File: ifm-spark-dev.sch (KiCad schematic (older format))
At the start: 21 parts, among them J1 CONN_01X03_MALE, J2 CONN_01X06, J3 CONN_01X02, J4 CONN_01X07, J5 CONN_01X03_MALE, SW1 PTS525-SM15, U1 STM32F030x4, Y1 8MHz

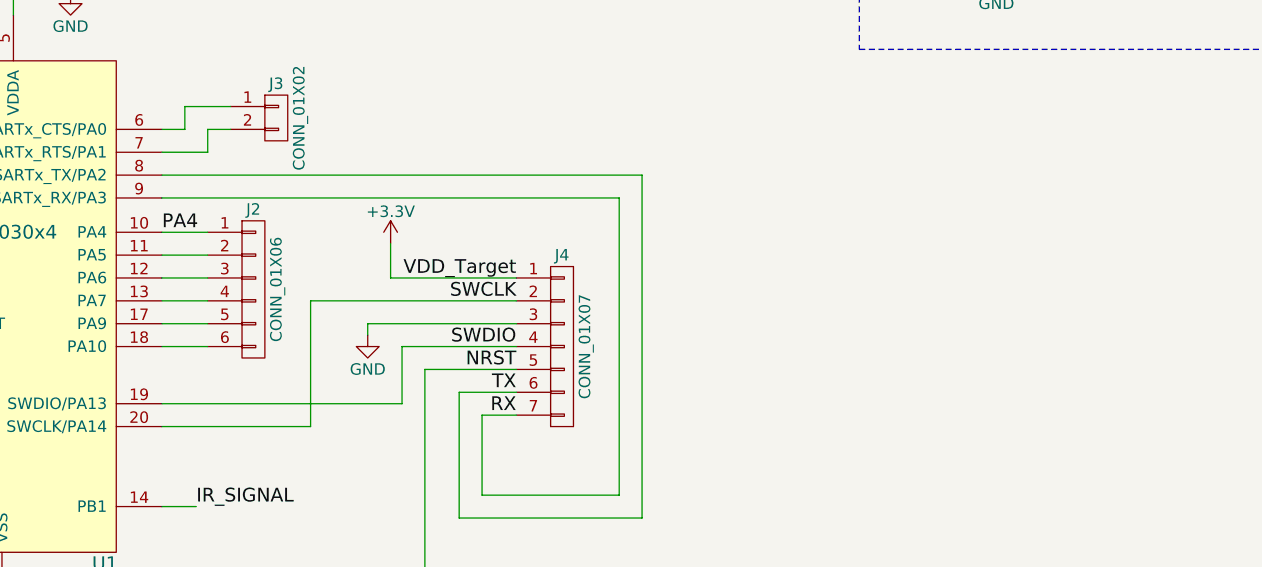
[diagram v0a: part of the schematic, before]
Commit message: Re-order extra GPIO pins for easier layout
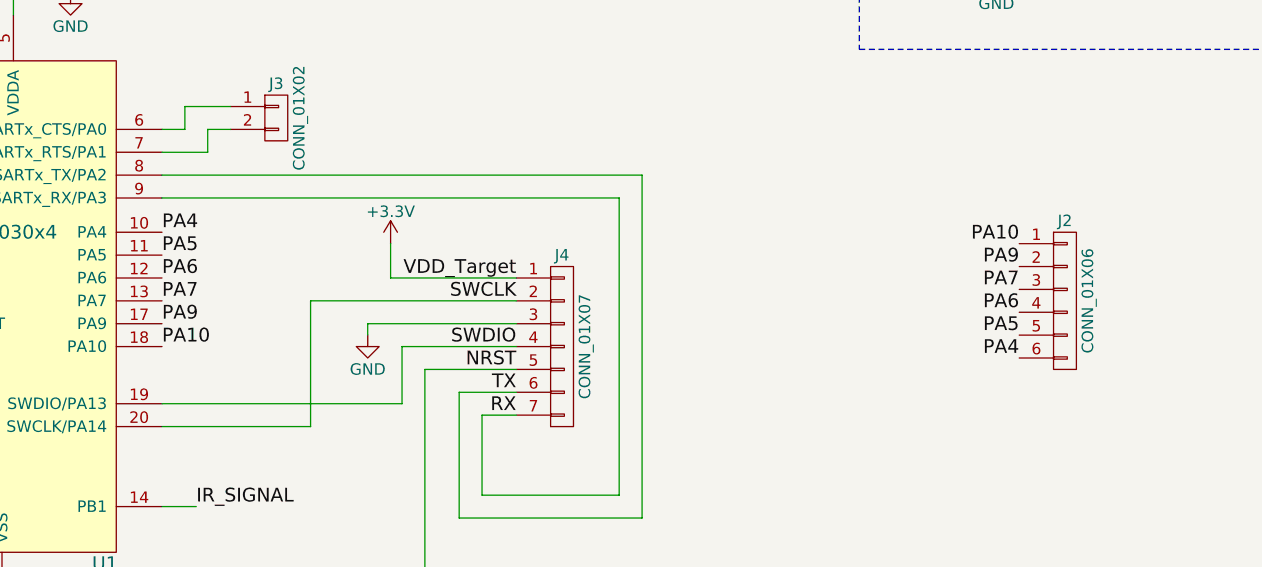
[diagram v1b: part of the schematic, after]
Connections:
- net PA4: now also J2.6 (P6); no longer J2.1 (P1)
- net PA5: now reaches U1.11 (PA5)
- net PA5: now also J2.5 (P5); no longer J2.2 (P2)
- net PA6: now reaches U1.12 (PA6)
- net PA6: now also J2.4 (P4); no longer J2.3 (P3)
- net PA7: now reaches U1.13 (PA7)
- net PA7: now also J2.3 (P3); no longer J2.4 (P4)
- net PA9: now reaches U1.17 (PA9)
- net PA9: now also J2.2 (P2); no longer J2.5 (P5)
- net PA10: now reaches U1.18 (PA10)
- net PA10: now also J2.1 (P1); no longer J2.6 (P6)
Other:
- moved on the sheet: J2
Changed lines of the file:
@@
 L CONN_01X06 J2
 U 1 1 592BABFC
-P 6650 3400
-F 0 "J2" H 6650 3750 50  0000 C CNN
-F 1 "CONN_01X06" V 6750 3400 50  0000 C CNN
-F 2 "Pin_Headers:Pin_Header_Straight_1x06_Pitch2.54mm" H 6650 3400 50  0001 C CNN
-F 3 "" H 6650 3400 50  0001 C CNN
-	1    6650 3400
-	1    0    0    -1
-$EndComp
-Wire Wire Line
-	6250 3150 6450 3150
-Wire Wire Line
-	6250 3250 6450 3250
-Wire Wire Line
-	6250 3350 6450 3350
-Wire Wire Line
-	6250 3450 6450 3450
-Wire Wire Line
-	6250 3550 6450 3550
-Wire Wire Line
-	6250 3650 6450 3650
+P 10200 3450
+F 0 "J2" H 10200 3800 50  0000 C CNN
+F 1 "CONN_01X06" V 10300 3450 50  0000 C CNN
+F 2 "Pin_Headers:Pin_Header_Straight_1x06_Pitch2.54mm" H 10200 3450 50  0001 C CNN
+F 3 "" H 10200 3450 50  0001 C CNN
+	1    10200 3450
+	1    0    0    -1
+$EndComp
 $Comp
 L R R4
@@
 Connection ~ 4200 3650
 Connection ~ 4200 3350
+Text Label 10000 3700 2    60   ~ 0
+PA4
+Text Label 6250 3250 0    60   ~ 0
+PA5
+Text Label 6250 3350 0    60   ~ 0
+PA6
+Text Label 6250 3450 0    60   ~ 0
+PA7
+Text Label 6250 3550 0    60   ~ 0
+PA9
+Text Label 6250 3650 0    60   ~ 0
+PA10
+Text Label 10000 3600 2    60   ~ 0
+PA5
+Text Label 10000 3500 2    60   ~ 0
+PA6
+Text Label 10000 3400 2    60   ~ 0
+PA7
+Text Label 10000 3300 2    60   ~ 0
+PA9
+Text Label 10000 3200 2    60   ~ 0
+PA10
 $EndSCHEMATC
